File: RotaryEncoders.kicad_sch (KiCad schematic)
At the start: 14 parts, among them U201 PEC11H-4025F-S0016, U202 PEC11H-4025F-S0016

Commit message: Fixed library links
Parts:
- U201, U202: footprint PEC11H4025FS0016 -> footprints:PEC11H4025FS0016
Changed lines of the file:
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@@
 			)
 		)
-		(property "Footprint" "PEC11H4025FS0016"
+		(property "Footprint" "footprints:PEC11H4025FS0016"
 			(at 121.92 130.48 0)
 			(effects
@@
 			)
 		)
-		(property "Footprint" "PEC11H4025FS0016"
+		(property "Footprint" "footprints:PEC11H4025FS0016"
 			(at 55.88 130.48 0)
 			(effects

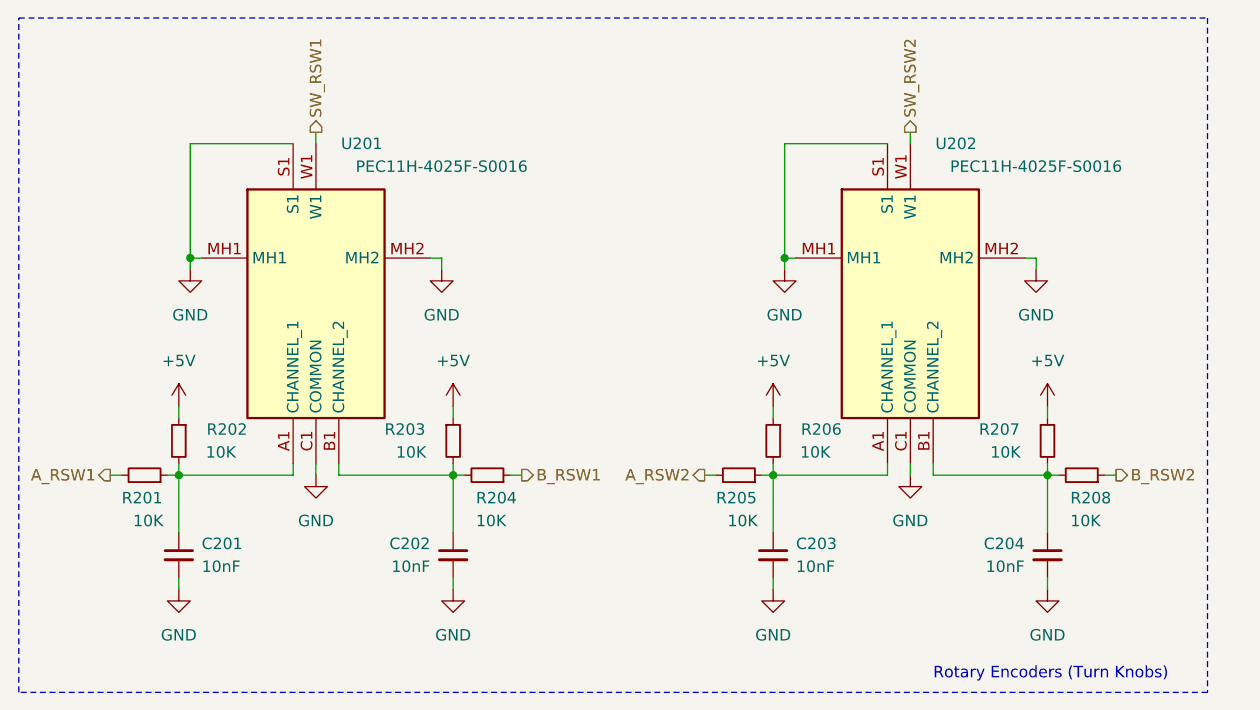
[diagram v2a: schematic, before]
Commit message: Fixed wiring for OLED display, push button for rotary & added chips for programming via USB C
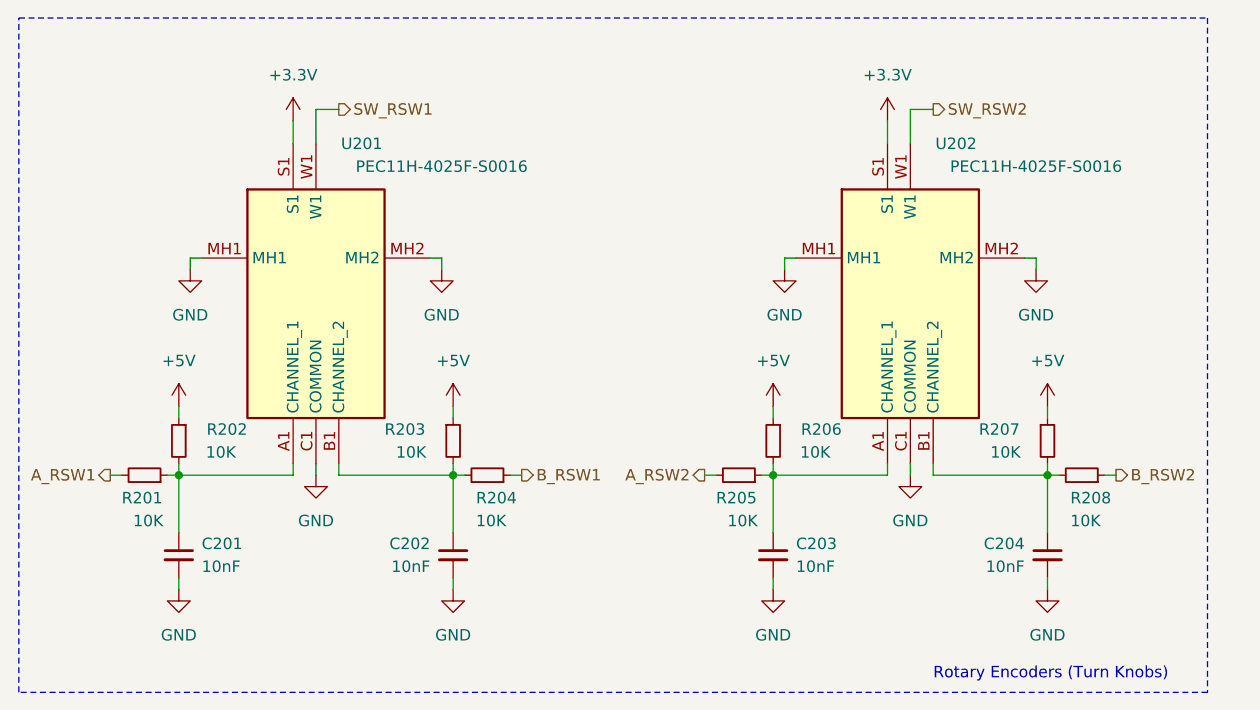
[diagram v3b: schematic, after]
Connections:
- net GND: no longer U201.S1, U202.S1
- new net +3.3V: U201.S1, U202.S1
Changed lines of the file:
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@@
-	)
-	(junction
-		(at 99.06 40.64)
-		(diameter 0)
-		(color 0 0 0 0)
 	)
 	(junction
@@
 	)
 	(junction
-		(at 33.02 40.64)
-		(diameter 0)
-		(color 0 0 0 0)
-	)
-	(junction
 		(at 62.23 64.77)
 		(diameter 0)
@@
 	(wire
 		(pts
-			(xy 44.45 27.94) (xy 33.02 27.94)
+			(xy 44.45 25.4) (xy 44.45 27.94)
 		)
 		(stroke
@@
 	(wire
 		(pts
-			(xy 113.03 26.67) (xy 113.03 27.94)
-		)
-		(stroke
-			(width 0)
-			(type default)
-		)
-	)
-	(wire
-		(pts
 			(xy 90.17 64.77) (xy 91.44 64.77)
 		)
@@
 	(wire
 		(pts
-			(xy 99.06 27.94) (xy 99.06 40.64)
+			(xy 110.49 25.4) (xy 110.49 27.94)
 		)
 		(stroke
@@
 	(wire
 		(pts
+			(xy 113.03 24.13) (xy 113.03 27.94)
+		)
+		(stroke
+			(width 0)
+			(type default)
+		)
+	)
+	(wire
+		(pts
 			(xy 49.53 64.77) (xy 62.23 64.77)
 		)
@@
 	(wire
 		(pts
+			(xy 49.53 24.13) (xy 46.99 24.13)
+		)
+		(stroke
+			(width 0)
+			(type default)
+		)
+	)
+	(wire
+		(pts
 			(xy 49.53 63.5) (xy 49.53 64.77)
 		)
@@
 	(wire
 		(pts
+			(xy 46.99 24.13) (xy 46.99 27.94)
+		)
+		(stroke
+			(width 0)
+			(type default)
+		)
+	)
+	(wire
+		(pts
 			(xy 128.27 76.2) (xy 128.27 77.47)
 		)
@@
 	(wire
 		(pts
-			(xy 46.99 26.67) (xy 46.99 27.94)
-		)
-		(stroke
-			(width 0)
-			(type default)
-		)
-	)
-	(wire
-		(pts
 			(xy 44.45 63.5) (xy 44.45 64.77)
 		)
@@
 	(wire
 		(pts
-			(xy 33.02 27.94) (xy 33.02 40.64)
-		)
-		(stroke
-			(width 0)
-			(type default)
-		)
-	)
-	(wire
-		(pts
 			(xy 97.79 57.15) (xy 97.79 58.42)
 		)
@@
 	(wire
 		(pts
-			(xy 110.49 27.94) (xy 99.06 27.94)
-		)
-		(stroke
-			(width 0)
-			(type default)
-		)
-	)
-	(wire
-		(pts
 			(xy 46.99 63.5) (xy 46.99 64.77)
 		)
@@
 		(pts
 			(xy 31.75 64.77) (xy 31.75 71.12)
+		)
+		(stroke
+			(width 0)
+			(type default)
+		)
+	)
+	(wire
+		(pts
+			(xy 115.57 24.13) (xy 113.03 24.13)
 		)
 		(stroke
@@
 	(hierarchical_label "SW_RSW1"
 		(shape output)
-		(at 46.99 26.67 90)
+		(at 49.53 24.13 0)
 		(fields_autoplaced yes)
 		(effects
@@
 	(hierarchical_label "SW_RSW2"
 		(shape output)
-		(at 113.03 26.67 90)
+		(at 115.57 24.13 0)
 		(fields_autoplaced yes)
 		(effects
@@
 	)
 	(symbol
+		(lib_id "power:+3.3V")
+		(at 44.45 25.4 0)
+		(unit 1)
+		(exclude_from_sim no)
+		(in_bom yes)
+		(on_board yes)
+		(dnp no)
+		(fields_autoplaced yes)
+		(property "Reference" "#PWR0215"
+			(at 44.45 29.21 0)
+			(effects
+				(font
+					(size 1.27 1.27)
+				)
+				(hide yes)
+			)
+		)
+		(property "Value" "+3.3V"
+			(at 44.45 20.32 0)
+			(effects
+				(font
+					(size 1.27 1.27)
+				)
+			)
+		)
+		(property "Footprint" ""
+			(at 44.45 25.4 0)
+			(effects
+				(font
+					(size 1.27 1.27)
+				)
+				(hide yes)
+			)
+		)
+		(property "Datasheet" ""
+			(at 44.45 25.4 0)
+			(effects
+				(font
+					(size 1.27 1.27)
+				)
+				(hide yes)
+			)
+		)
+		(property "Description" ""
+			(at 44.45 25.4 0)
+			(effects
+				(font
+					(size 1.27 1.27)
+				)
+				(hide yes)
+			)
+		)
+		(pin "1"
+		)
+		(instances
+			(project "Universal Control Box"
+				(path "/0356e092-4721-4291-8799-df5160707ecc/cf652236-89fd-42e9-8b11-4ef709efb5a0"
+					(reference "#PWR0215")
+					(unit 1)
+				)
+			)
+		)
+	)
+	(symbol
 		(lib_id "Device:R_Small")
 		(at 128.27 60.96 0)
@@
 					(unit 1)
 				)
+			)
+		)
+	)
+	(symbol
+		(lib_id "power:+3.3V")
+		(at 110.49 25.4 0)
+		(unit 1)
+		(exclude_from_sim no)
+		(in_bom yes)
+		(on_board yes)
+		(dnp no)
+		(fields_autoplaced yes)
+		(property "Reference" "#PWR0216"
+			(at 110.49 29.21 0)
+			(effects
+				(font
+					(size 1.27 1.27)
+				)
+				(hide yes)
+			)
+		)
+		(property "Value" "+3.3V"
+			(at 110.49 20.32 0)
+			(effects
+				(font
+					(size 1.27 1.27)
+				)
+			)
+		)
+		(property "Footprint" ""
+			(at 110.49 25.4 0)
+			(effects
+				(font
+					(size 1.27 1.27)
+				)
+				(hide yes)
+			)
+		)
+		(property "Datasheet" ""
+			(at 110.49 25.4 0)
+			(effects
+				(font
+					(size 1.27 1.27)
+				)
+				(hide yes)
+			)
+		)
+		(property "Description" ""
+			(at 110.49 25.4 0)
+			(effects
+				(font
+					(size 1.27 1.27)
+				)
+				(hide yes)
+			)
+		)
+		(pin "1"
+		)
+		(instances
+			(project "Universal Control Box"
+				(path "/0356e092-4721-4291-8799-df5160707ecc/cf652236-89fd-42e9-8b11-4ef709efb5a0"
+					(reference "#PWR0216")
+					(unit 1)
+				)
